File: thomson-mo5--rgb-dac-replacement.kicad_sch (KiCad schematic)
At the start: 23 parts, among them J1 Input, J2 Output, Q1 2N3904, Q2 2N3904, Q3 2N3904

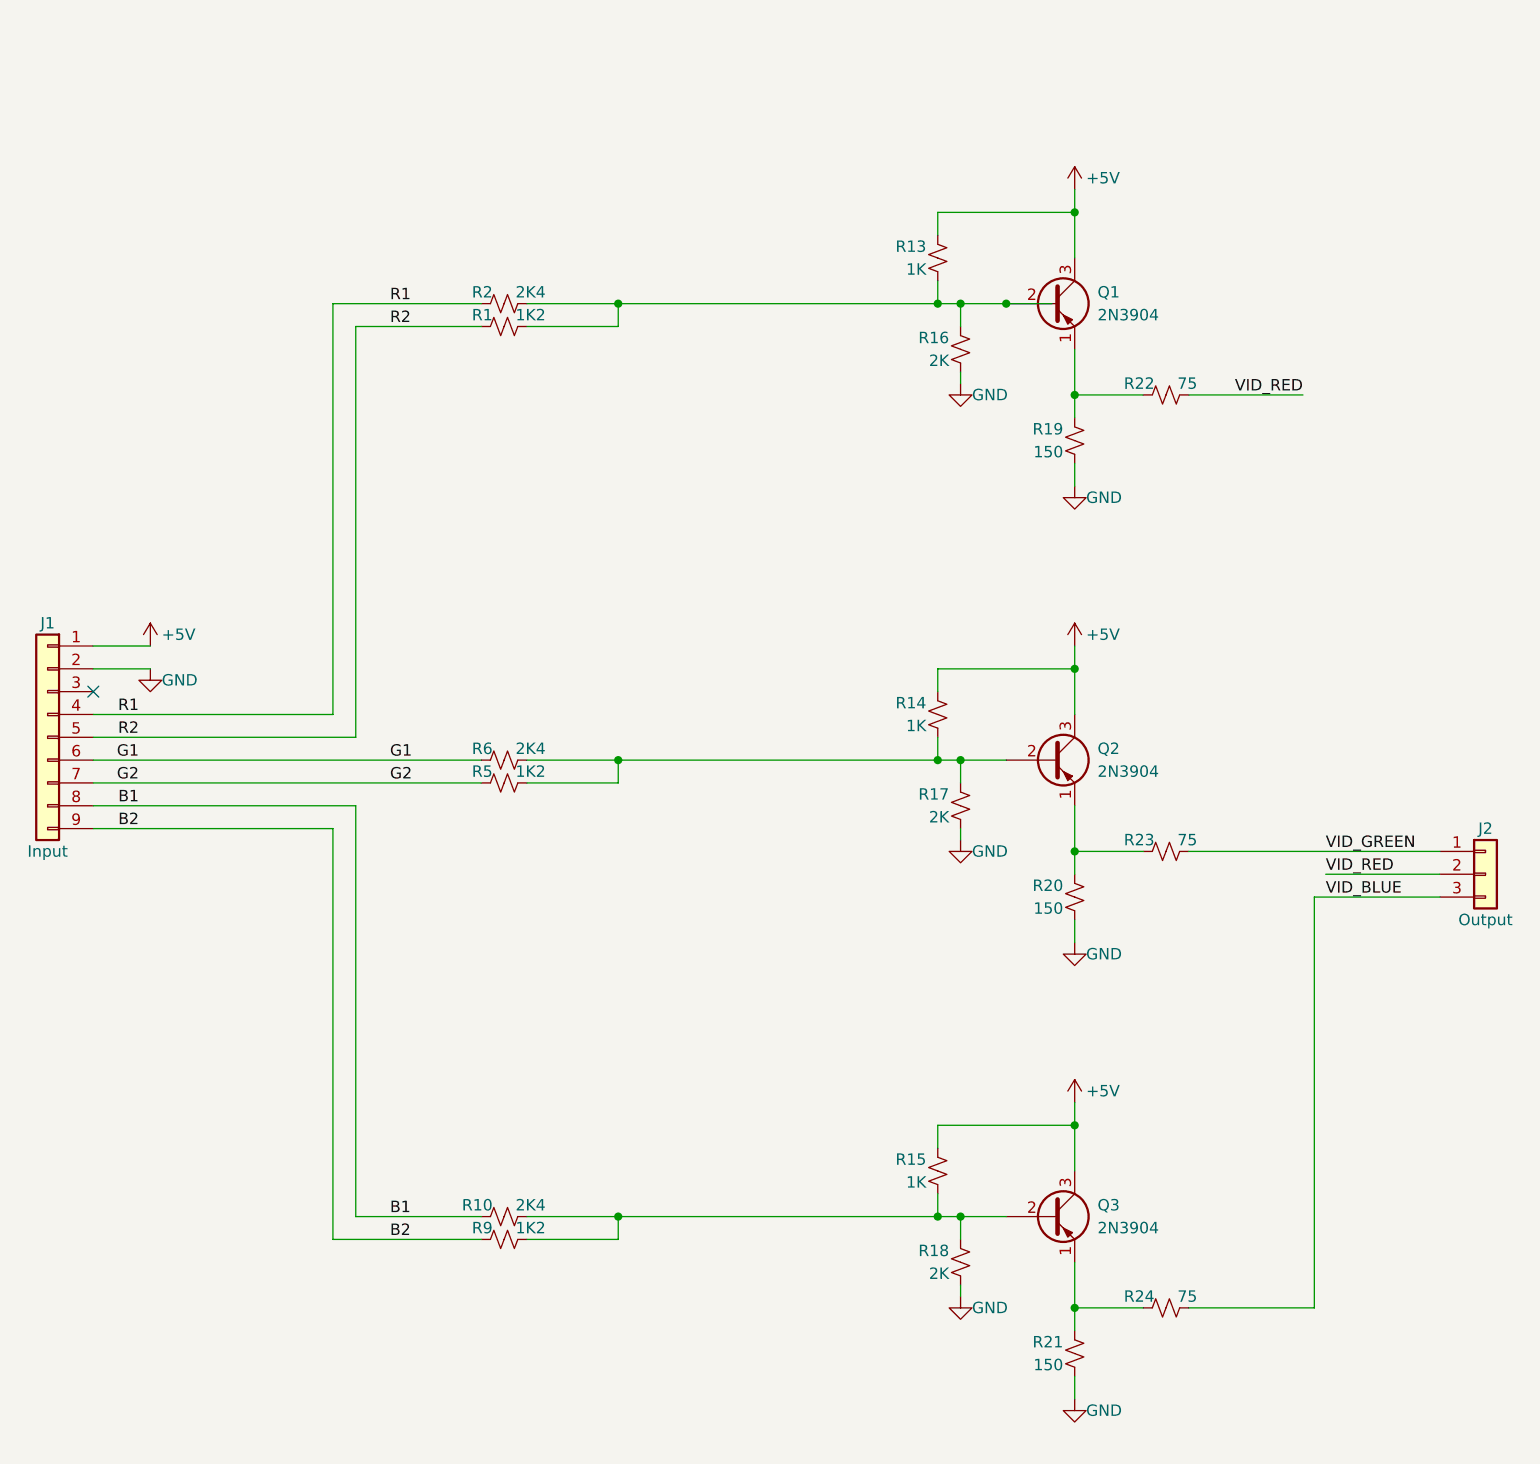
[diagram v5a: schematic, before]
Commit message: [pcb] applied schematic change, and shrinked the required size
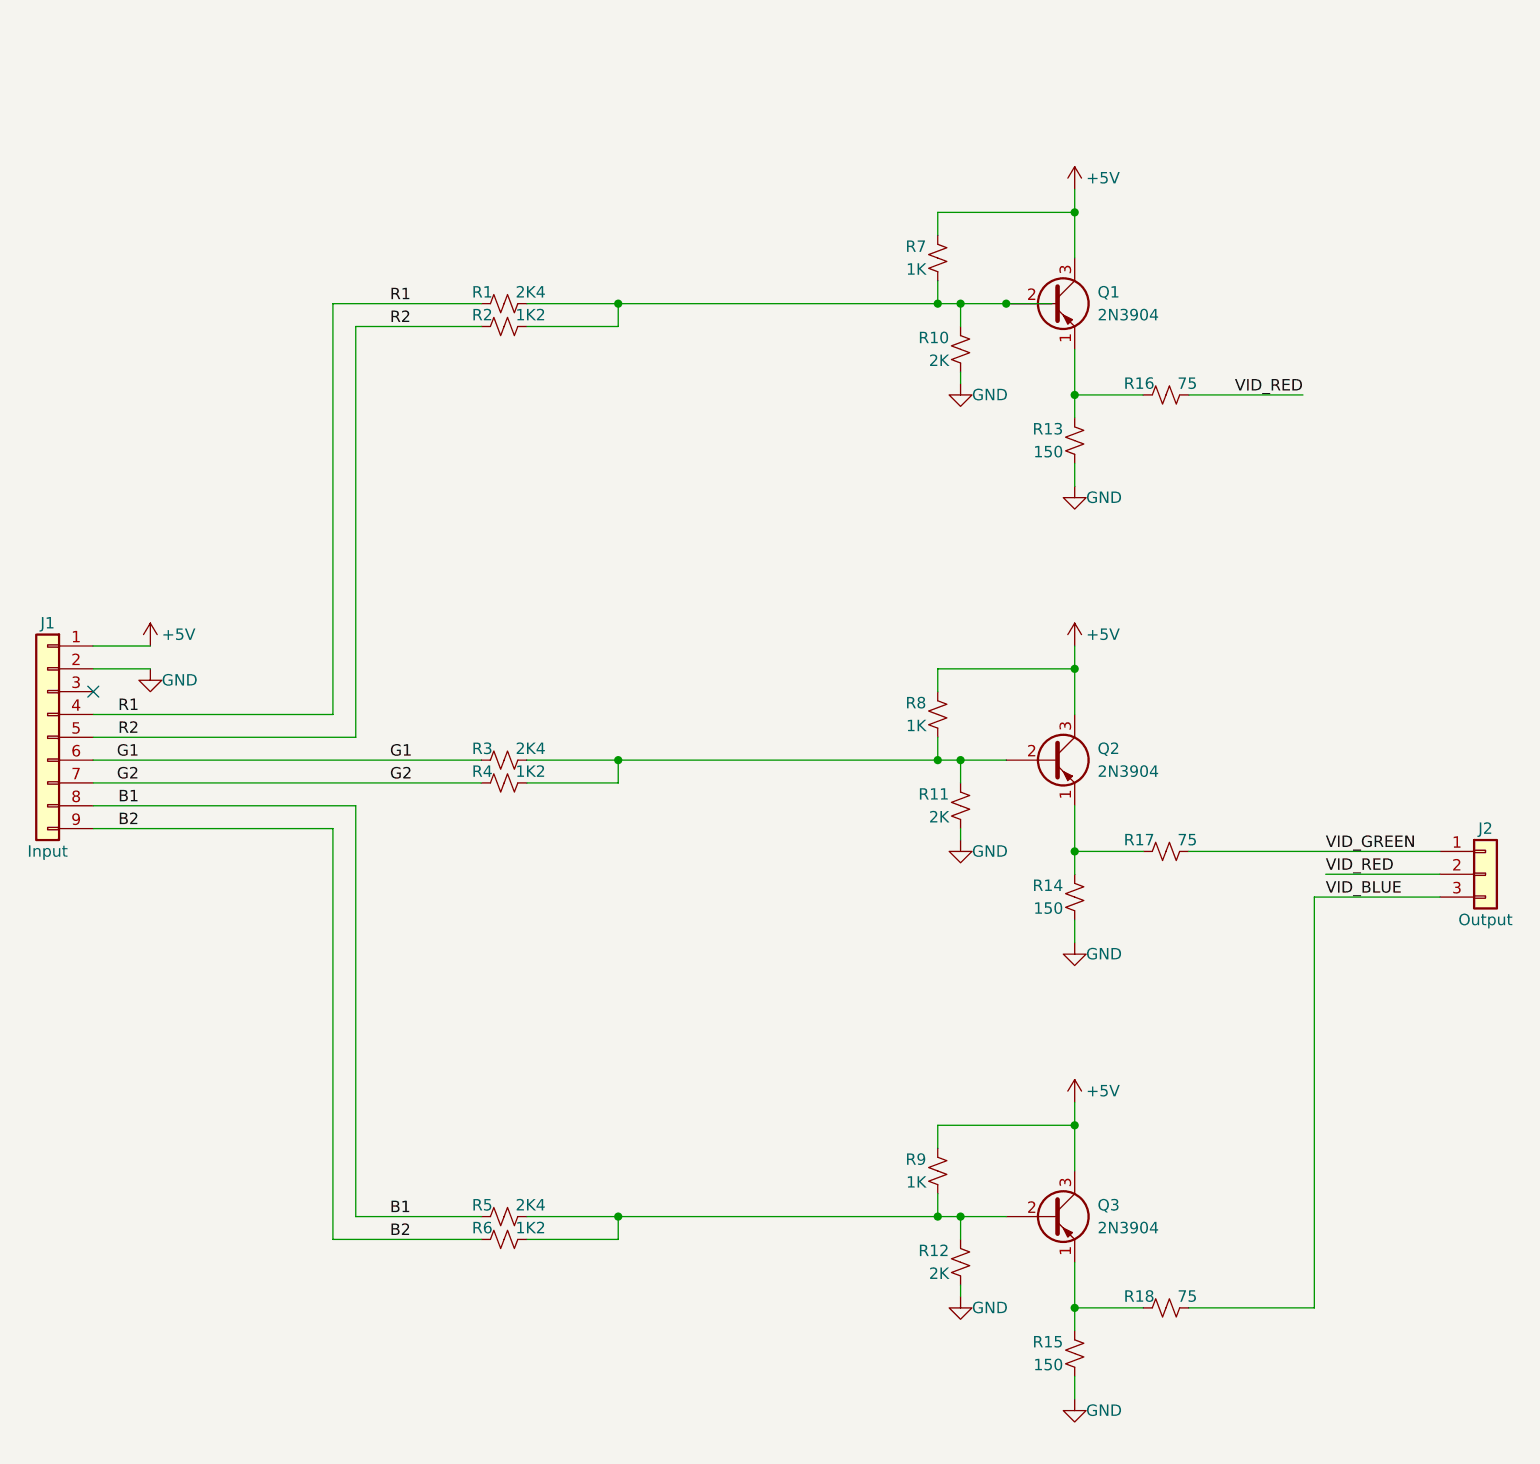
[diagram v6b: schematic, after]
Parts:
- renumbered R2 to R1, R16 to R10, R17 to R11, R18 to R12, R19 to R13, R20 to R14, R21 to R15, R22 to R16, R23 to R17, R24 to R18, R1 to R2, R6 to R3, R5 to R4, R10 to R5, R9 to R6, R13 to R7, R14 to R8, R15 to R9
